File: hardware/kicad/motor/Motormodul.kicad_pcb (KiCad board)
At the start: 2 copper layers, 75 x 65 mm, 63 parts, among them J100 Stapelstecker links, Pico-Pin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, J101 Kettenstecker, Buchse oben (S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, J102 Kettenstecker, Stift unten (S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, J103 Leistungsstecker, Buchse oben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, J104 Leistungsstecker, Stift unten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, J105 Stapelstecker rechts, Pico-Pi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, J3 Notaus-Ruhestrom, J5 Motor-Klemme, J90 Versorgung Eingang, J95 Randpads GPIO, unbestueckt (T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, J96 Randpads Versorgung: 2x 3V3 +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, Q90 IRFR5305, U1 DRV8876PWPR, U100 STM32C011F6P6, U101 SN74LVC1G175, U102 SN74LVC2G00DCUR, U103 SN74LVC1G08, U3 SN74LVC1G08, U4 PC817, U5 PC817, U6 SN74LVC1G07, U7 SN74LVC1G07, U90 K7805-1000R3

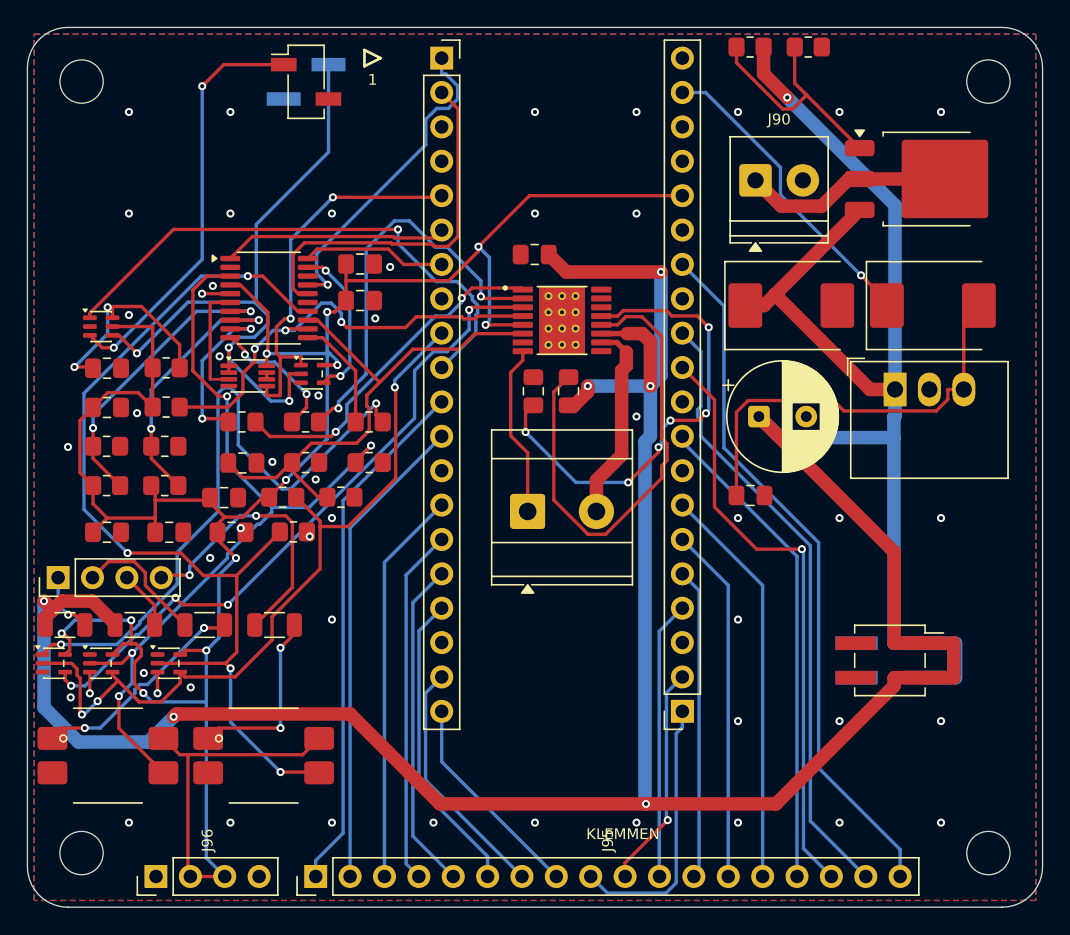
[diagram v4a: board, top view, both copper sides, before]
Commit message: Aufgabe 7b: Motormodul neu verlegt auf der vertragstreuen Platzierung (Fix-Runde 2)
Wurf t7, bester aus 26 Wuerfen der Laeufe r, s und t.

  kicad-cli pcb drc --severity-error --exit-code-violations
    Found 0 violations
    Found 2 unconnected items

Die zwei Posten, vollstaendig:
  1. /CPL  C10-2 <-> U1-14 -- die eine Netz-Luecke.
  2. eine GND-Insel in der Notaus-Ecke (F.Cu x 6,9..11,0 y 46,1..49,5,
     B.Cu x 7,7..10,6 y 45,2..51,5). Der masseheiler-Wachhund bleibt
     deshalb ROT; er heilte in diesem Lauf sieben Stuecke und meldet
     diese eine Gruppe als ohne freien Heilpunkt.

steckerprobe.py: VOLLSTAENDIG GRUEN, alle elf Zeilen -- die sechs
Vertragsstecker, Umriss, Bohrungen, Lochbild, Kennzeichnung UND
"Verdreht 46 Landepunkte, alle >= 1.5 mm von freiliegendem Kupfer".

pcb_checks.py: 133 Vias, alle beidseitig angebunden; ANTENNE_FREI auf
F.Cu kupferfrei.

tests/run_all.py: Rot-Liste unveraendert die vier erwarteten.

/CPL IST NICHT ERREICHT und das ist gemessen, nicht aufgegeben: die
Verbindung blieb in ALLEN 26 Wuerfen offen. Sie ist die fuenfte in einer
Gasse, die nur vier traegt -- durch die 4,39 mm zwischen U1s Ostpadkante
und der J105-Reihe muessen /Out2 und /+24V in Leistungsbreite plus
/VCP, /CPH und /CPL. Drei Auswege von Hand nachgerechnet und alle drei
widerlegt: suedlich zwischen U1 und /VCPs Ausfahrt bleiben 0,325 mm
(noetig 0,65), westlich sperrt /Out1 die Zufahrt zu C10, und der Spalt
zwischen C10s beiden Pads ist 0,625 mm (noetig 0,65). Herleitung im
Bericht, Abschnitt G5; die Abhilfe ist eine Platzierungsentscheidung
(C9/C10 oder U1), keine Verlegung.

Co-Authored-By: Claude Fable 5 <noreply@anthropic.com>
Claude-Session: https://claude.ai/code/session_01KDus95JJwCeRuwccgBWEi5
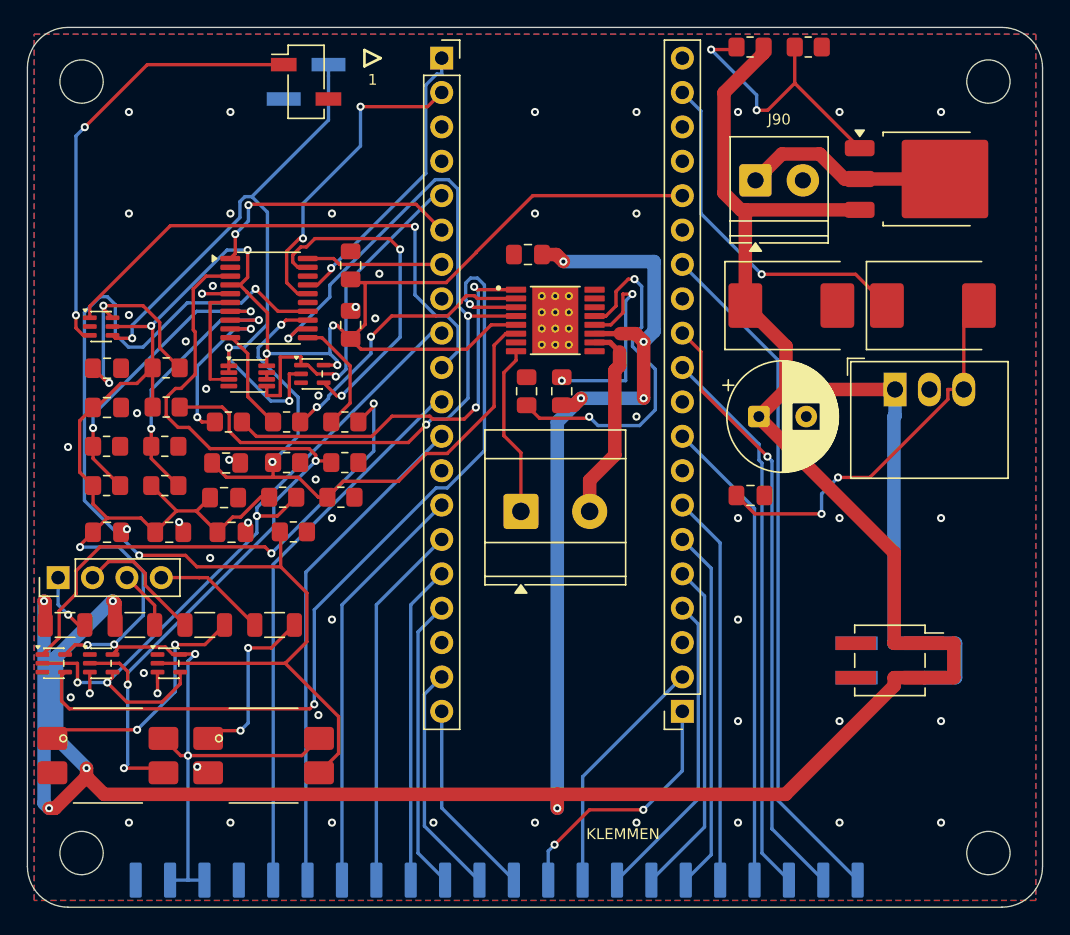
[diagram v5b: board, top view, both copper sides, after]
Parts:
- J95: value Randpads GPIO, unbestueckt (THT-Loetpad) -> Randpads GPIO, unbestueckt (SMD-Loetpad, Rueckseite); footprint PinHeader_1x18_P2.54mm_Vertical -> Randpad_Reihe_1x18; moved to B.Cu
- J96: value Randpads Versorgung: 2x 3V3 + 2x GND, unbestueckt (THT-Loetpad) -> Randpads Versorgung: 2x 3V3 + 2x GND, unbestueckt (SMD-Loetpad, Rueckseite); footprint PinHeader_1x04_P2.54mm_Vertical -> Randpad_Reihe_1x04; moved to B.Cu
- moved J95 3.15 mm to (18.2, 63.0), turned to 180 degrees
- moved C16 1.93 mm to (23.9, 22.0), turned to 90 degrees
- moved R20 1.80 mm to (23.4, 32.1)
- moved R9 1.80 mm to (23.4, 29.1)
- moved J96 1.52 mm to (8.00, 63.0), turned to 180 degrees
- moved R5 1.40 mm to (19.1, 32.1)
- moved R8 1.40 mm to (19.1, 29.1)
- moved C13 1.20 mm to (14.7, 32.2)
- moved R7 1.00 mm to (14.8, 29.1)
- moved C14 0.71 mm to (23.9, 17.6), turned to 90 degrees
- moved C10 0.50 mm to (36.9, 26.9)
- moved C11 0.50 mm to (37.0, 16.8)
- moved C9 0.50 mm to (39.5, 26.9)
- moved J5 0.50 mm to (36.5, 35.8)
- moved U1 0.50 mm to (39.0, 21.6)
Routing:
- net /NFAULT: track 33.2 -> 63.7 mm
- net /VCP: track 36.4 -> 16.1 mm, vias 0 -> 2
- net /U1_NSLEEP: track 49.5 -> 64.9 mm, vias 4 -> 2
- net /BOOT0: track 11.7 -> 24.9 mm
- net /KREIS2_B: track 20.9 -> 8.36 mm, vias 2 -> 0
- net 3V3: track 188.7 -> 176.5 mm, vias 11 -> 10
- net /SCHLEIFE_2: track 72.1 -> 83.6 mm, vias 4 -> 2
- net /NSLEEP_GATTER: track 48.8 -> 38.6 mm
- net /U1_PH_IN2: track 29.9 -> 20.8 mm
- net /CPH: track 35.1 -> 26.3 mm, vias 6 -> 2
- net /IPROPI: track 39.4 -> 47.3 mm, vias 0 -> 2
- net /U1_EN_IN1: track 25.7 -> 31.1 mm
- net /FLASH_RX: track 27.9 -> 23.7 mm, vias 0 -> 2
- net /SEL_OUT: track 49.3 -> 52.9 mm
- net /Q90_GATE: track 17.6 -> 20.9 mm, vias 0 -> 2
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
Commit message: Aufgabe 7b: Motormodul verlegt -- alle Bauteilnetze geschlossen (Wurf x2)
Bester aus 14 Wuerfen des Laufs x, ausgewaehlt nach dem, was funktional
zaehlt: KEINE einzige Netz-Luecke mehr.

  kicad-cli pcb drc --severity-error --exit-code-violations
    Found 0 violations
    Found 3 unconnected items

Die drei Posten sind AUSSCHLIESSLICH Zone-gegen-Zone -- kein Pad, kein
Netz. Jede Verbindung zwischen zwei Bauteilen ist verlegt; uebrig
bleiben drei Fragmente des Masseflaechen-Gusses, die nicht an den
Hauptguss angebunden sind (masseheiler-Wachhund nennt sie: F.Cu
6,4..10,6 x 46,1..49,5 / 13,8..15,8 x 26,3..27,5 / 27,2..35,0 x
16,6..21,0 und B.Cu 7,4..10,4 x 44,8..51,3 / 29,8..32,6 x 17,4..23,3).
Das ist ein EMC- und Fertigungsmangel, kein Funktionsfehler: die
GND-PADS selbst haengen alle am Netz, sonst wuerde die DRC sie
namentlich melden.

steckerprobe.py: alle elf Zeilen gruen, einschliesslich
"Verdreht 46 Landepunkte, alle >= 1.5 mm von freiliegendem Kupfer".

pcb_checks.py: 151 Vias, alle beidseitig angebunden; ANTENNE_FREI auf
F.Cu kupferfrei.

tests/run_all.py: Rot-Liste unveraendert die vier erwarteten.

Zum Vergleich der Ausgangslage dieser Aufgabe: 25 DRC-Verletzungen und
15 offene Posten, davon 21 Verletzungen allein aus der Vorverdrahtung.

Co-Authored-By: Claude Fable 5 <noreply@anthropic.com>
Claude-Session: https://claude.ai/code/session_01KDus95JJwCeRuwccgBWEi5
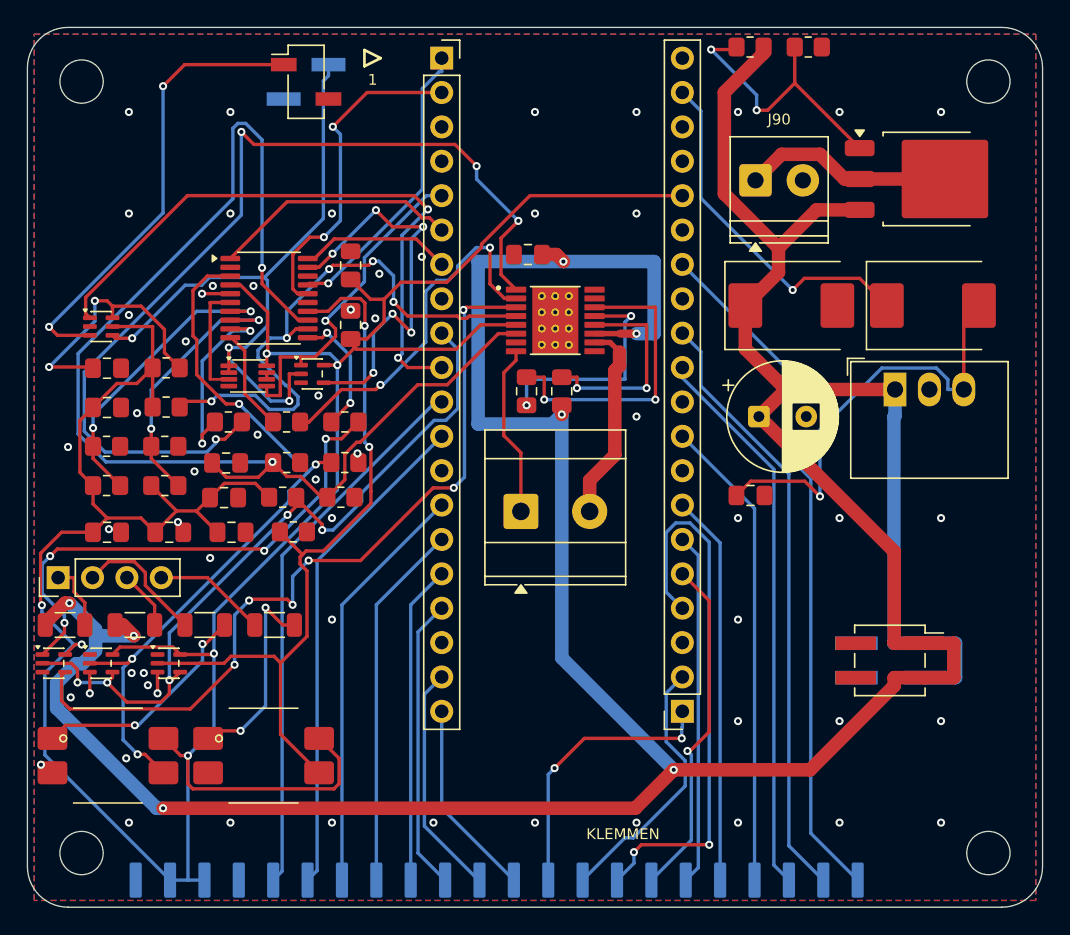
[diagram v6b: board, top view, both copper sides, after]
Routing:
- net /IPROPI: track 47.3 -> 91.1 mm
- net 3V3: track 176.5 -> 216.9 mm, vias 10 -> 6
- net /U1_EN_IN1: track 31.1 -> 70.1 mm, vias 2 -> 4
- net /SCHLEIFE_2: track 83.6 -> 56.6 mm
- net /CPL: track 0.00 -> 22.5 mm, vias 0 -> 2
- net /NFAULT: track 63.7 -> 42.7 mm, vias 3 -> 5
- net /GP18: track 23.1 -> 40.9 mm, vias 0 -> 2
- net /CPH: track 26.3 -> 16.7 mm
- net /SCHLEIFE_1: track 63.2 -> 55.4 mm, vias 3 -> 4
- net /U1_PH_IN2: track 20.8 -> 26.8 mm
- net /SEL_CLK: track 40.1 -> 45.9 mm, vias 1 -> 2
- net /U1_NSLEEP: track 64.9 -> 59.4 mm, vias 2 -> 6
- net /BOOT0: track 24.9 -> 29.9 mm, vias 2 -> 6
- net /SEL_OUT: track 52.9 -> 49.4 mm
- net /+24V: track 272.0 -> 268.6 mm, vias 9 -> 7
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
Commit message: Aufgabe 7c: Motormodul neu verlegt mit dem Naehpunkt-Filter -- 0 Verletzungen, 0 offene Posten
Mit dem gefixten build.py neu gebaut (47 statt 48 Naehpunkte -- der
eine nachweislich fehlerhafte STITCH_EXTRA-Punkt ist raus) und neu
geworfen. Dieser Wurf routet restlos (freerouting: 0 unverlegt) und
masseheiler heilt alle sieben GND-Fragmente ueber einfache Vias (keine
Gegenlage-Bruecke noetig -- dieser Wurf war dafuer nicht eng genug).

kicad-cli pcb drc --severity-error --exit-code-violations
  Found 0 violations
  Found 0 unconnected items

masseheiler --nur-pruefen: alle Masseflaechen haengen zusammen
steckerprobe.py: alle elf Zeilen gruen
pcb_checks.py: 144 Vias beidseitig angebunden, ANTENNE_FREI kupferfrei

Keine Platzierung geaendert (nachgemessen: alle 63 Bauteile auf
identischer Position/Drehung wie zuvor) -- nur Verlegung und
Naehte sind neu.

Co-Authored-By: Claude Fable 5 <noreply@anthropic.com>
Claude-Session: https://claude.ai/code/session_01KDus95JJwCeRuwccgBWEi5
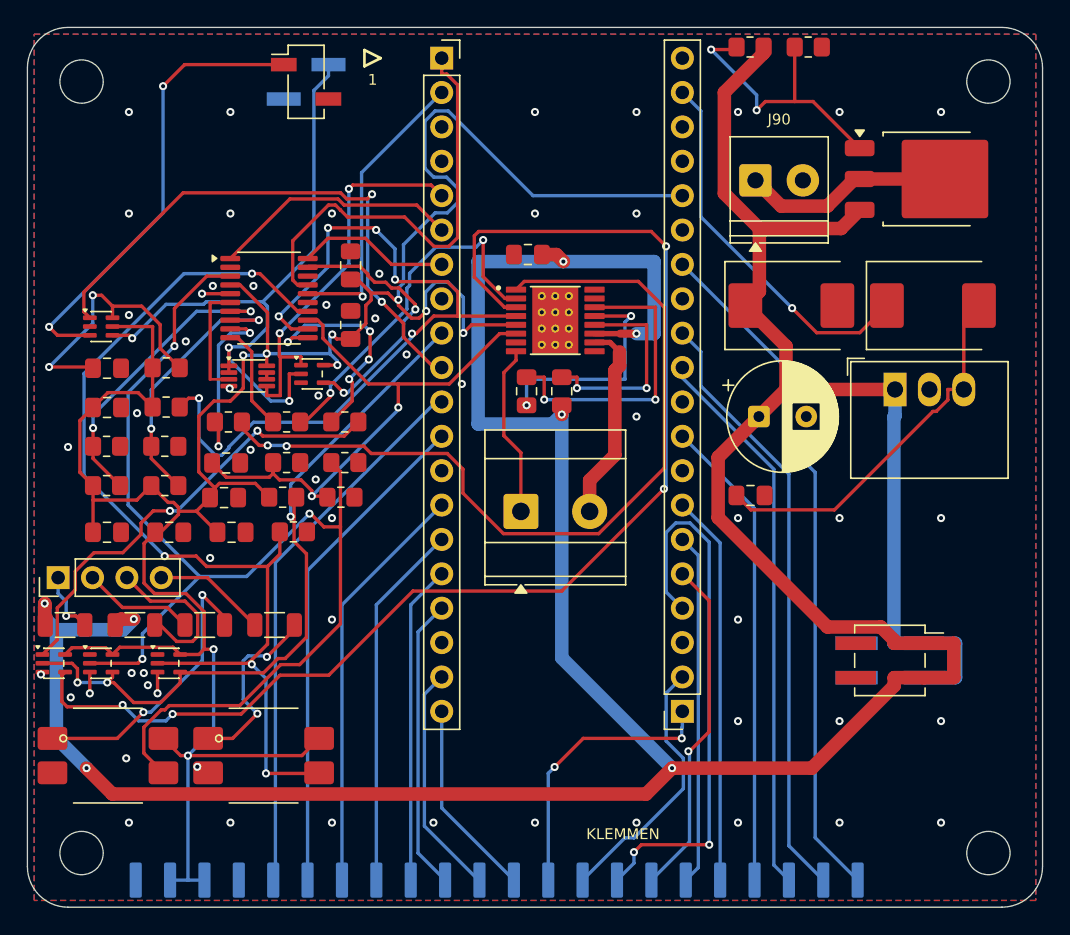
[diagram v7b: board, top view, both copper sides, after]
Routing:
- net /IPROPI: track 91.1 -> 41.2 mm
- net /U1_NSLEEP: track 59.4 -> 94.3 mm, vias 6 -> 4
- net /SCHLEIFE_1: track 55.4 -> 87.0 mm, vias 4 -> 3
- net 3V3: track 216.9 -> 195.4 mm, vias 6 -> 9
- net /SCHLEIFE_2: track 56.6 -> 74.7 mm, vias 2 -> 4
- net /NFAULT: track 42.7 -> 58.3 mm, vias 5 -> 6
- net /FLASH_TX: track 21.8 -> 32.9 mm, vias 1 -> 0
- net /BOOT0: track 29.9 -> 19.9 mm, vias 6 -> 2
- net /U1_EN_IN1: track 70.1 -> 61.8 mm, vias 4 -> 2
- net /KREIS2_A: track 4.35 -> 11.8 mm
- net /NSLEEP: track 9.48 -> 16.4 mm, vias 2 -> 4
- net /+24V: track 268.6 -> 273.5 mm
- net /NSLEEP_GATTER: track 38.0 -> 33.4 mm, vias 4 -> 2
- net /U4_LED_A: track 16.9 -> 21.2 mm
- net /+5V_LOKAL: track 32.3 -> 28.0 mm, vias 1 -> 0
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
